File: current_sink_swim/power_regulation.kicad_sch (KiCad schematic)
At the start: 6 parts, among them U3 TC1016

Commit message: assign footprints and start layout
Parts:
- C1, C2: footprint (none) -> Capacitor_SMD:C_0805_2012Metric_Pad1.18x1.45mm_HandSolder
- R2, R4, R5: footprint (none) -> Resistor_SMD:R_0805_2012Metric_Pad1.20x1.40mm_HandSolder
- U3: footprint (none) -> Package_SO:SOIC-8_3.9x4.9mm_P1.27mm
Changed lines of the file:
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@@
       (effects (font (size 1.27 1.27)) (justify left))
     )
-    (property "Footprint" "" (at 93.6498 66.04 0)
+    (property "Footprint" "Capacitor_SMD:C_0805_2012Metric_Pad1.18x1.45mm_HandSolder" (at 93.6498 66.04 0)
       (effects (font (size 1.27 1.27)) hide)
     )
@@
       (effects (font (size 1.27 1.27)))
     )
-    (property "Footprint" "" (at 121.285 95.25 0)
+    (property "Footprint" "Package_SO:SOIC-8_3.9x4.9mm_P1.27mm" (at 121.285 95.25 0)
       (effects (font (size 1.27 1.27) italic) hide)
     )
@@
       (effects (font (size 1.27 1.27)) (justify left))
     )
-    (property "Footprint" "" (at 153.9748 62.23 0)
+    (property "Footprint" "Capacitor_SMD:C_0805_2012Metric_Pad1.18x1.45mm_HandSolder" (at 153.9748 62.23 0)
       (effects (font (size 1.27 1.27)) hide)
     )
@@
       (effects (font (size 1.27 1.27)) (justify left))
     )
-    (property "Footprint" "" (at 107.315 78.105 0)
+    (property "Footprint" "Resistor_SMD:R_0805_2012Metric_Pad1.20x1.40mm_HandSolder" (at 107.315 78.105 0)
       (effects (font (size 1.27 1.27)) hide)
     )
@@
       (effects (font (size 1.27 1.27)) (justify left))
     )
-    (property "Footprint" "" (at 147.955 75.565 0)
+    (property "Footprint" "Resistor_SMD:R_0805_2012Metric_Pad1.20x1.40mm_HandSolder" (at 147.955 75.565 0)
       (effects (font (size 1.27 1.27)) hide)
     )
@@
       (effects (font (size 1.27 1.27)) (justify left))
     )
-    (property "Footprint" "" (at 147.955 62.23 0)
+    (property "Footprint" "Resistor_SMD:R_0805_2012Metric_Pad1.20x1.40mm_HandSolder" (at 147.955 62.23 0)
       (effects (font (size 1.27 1.27)) hide)
     )

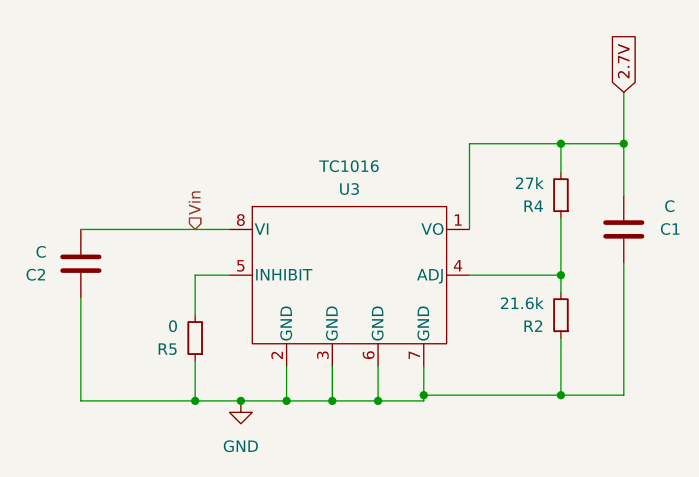
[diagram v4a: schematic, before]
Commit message: add part numbers and BOM
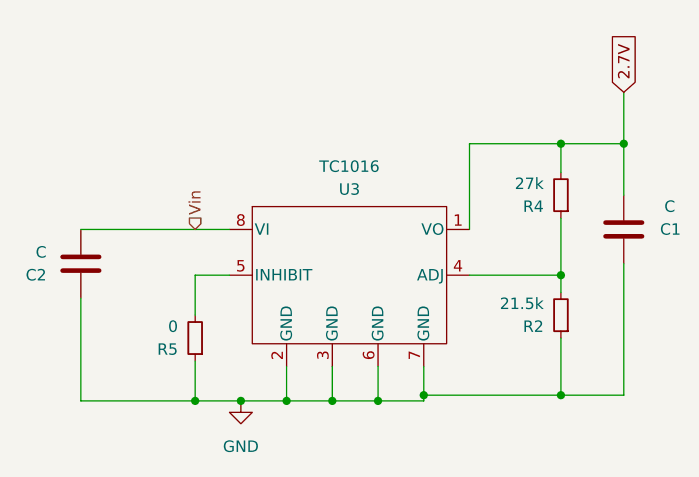
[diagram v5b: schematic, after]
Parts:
- R2: value 21.6k -> 21.5k
- U3: MPN (none) -> NCV2931CDR2G
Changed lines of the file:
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@@
       (effects (font (size 1.27 1.27) italic) hide)
     )
-    (property "Datasheet" "" (at 133.985 92.71 0)
+    (property "Datasheet" "https://www.onsemi.com/pdf/datasheet/lm2931-d.pdf" (at 133.985 92.71 0)
       (effects (font (size 1.27 1.27)) hide)
     )
-    (property "MPN" "" (at 125.095 66.04 0)
+    (property "MPN" "NCV2931CDR2G" (at 125.095 66.04 0)
       (effects (font (size 1.27 1.27)) hide)
     )
@@
       (effects (font (size 1.27 1.27)) (justify left))
     )
-    (property "Value" "21.6k" (at 146.05 74.295 0)
+    (property "Value" "21.5k" (at 146.05 74.295 0)
       (effects (font (size 1.27 1.27)) (justify left))
     )
